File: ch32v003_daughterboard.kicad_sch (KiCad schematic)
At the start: 7 parts, among them J1 Conn_02x05_Odd_Even, J2 Conn_01x03_Pin, P1 Header 7X2, P2 Header 7X2

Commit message: free SDIO + pot.
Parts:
- added RV1: Mouser PTN091-V05115K1B, symbol Device:R_Potentiometer
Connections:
- net GND: now also RV1.3
- net PD0: now also BAR1.1 (A)
- net PD1: no longer BAR1.1 (A)
- net PD3: now also RV1.2
- net VCC: now also RV1.1
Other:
- moved on the sheet: C1, C2, J1, J2, P1, P2

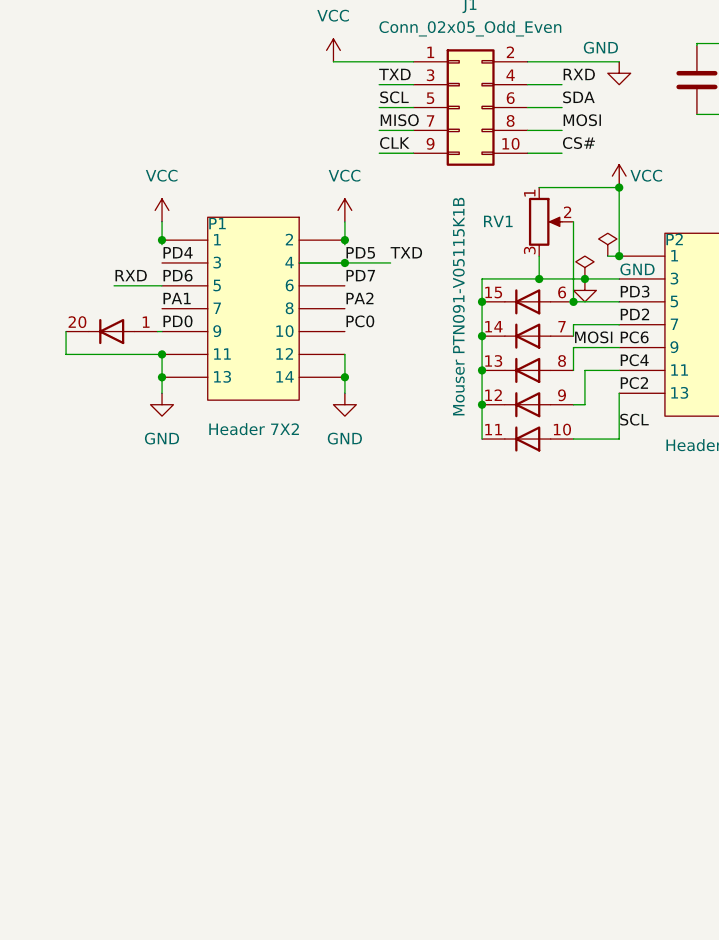
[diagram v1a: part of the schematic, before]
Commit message: add FTDI RS232-USB
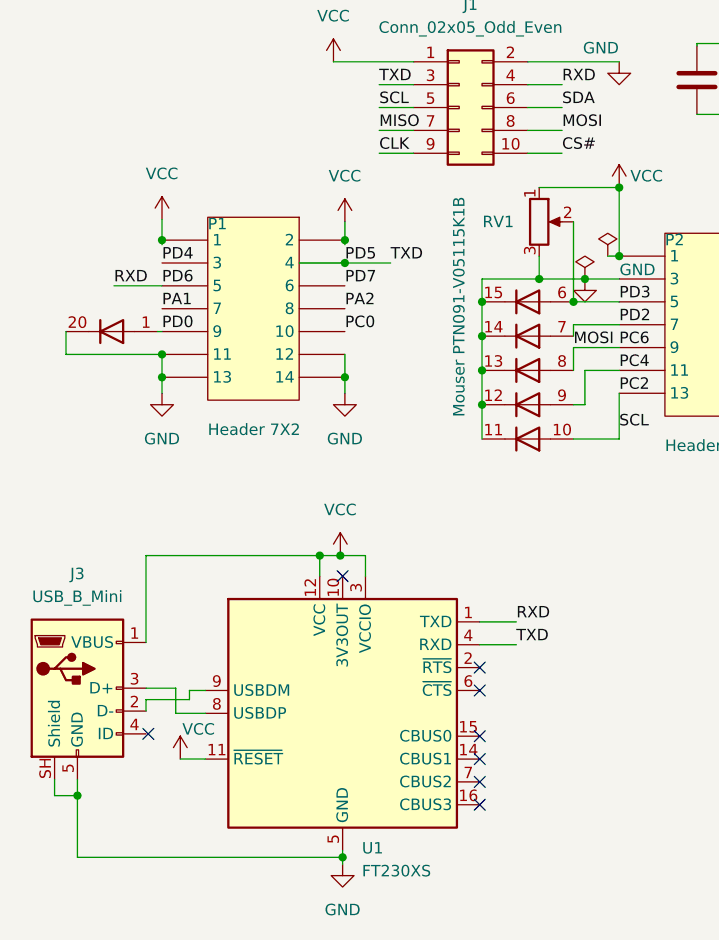
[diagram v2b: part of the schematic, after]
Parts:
- added J3: USB_B_Mini, Connector_USB:USB_Mini-B_Lumberg_2486_01_Horizontal, symbol Connector:USB_B_Mini
- added U1: FT230XS, Package_SO:SSOP-16_3.9x4.9mm_P0.635mm, symbol Interface_USB:FT230XS
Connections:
- net GND: now also J3.5 (GND), J3.SH (Shield), U1.13 (GND), U1.5 (GND)
- net PD5: now also U1.4 (RXD)
- net PD6: now also U1.1 (TXD)
- net VCC: now also J3.1 (VBUS), U1.11 (~{RESET}), U1.12 (VCC), U1.3 (VCCIO)
- new net: J3.3 (D+), U1.8 (USBDP)
- new net: J3.2 (D-), U1.9 (USBDM)
- no-connect marks 0 -> 8

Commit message: add push button
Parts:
- added R1: R, Resistor_SMD:R_0805_2012Metric_Pad1.20x1.40mm_HandSolder, symbol Device:R
- added SW1: SW_SPST, Button_Switch_SMD:SW_SPST_B3SL-1002P, symbol Switch:SW_SPST
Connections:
- net GND: now also SW1.2 (B)
- net PC0: now also R1.2, SW1.1 (A)
- net VCC: now also R1.1
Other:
- moved on the sheet: P1

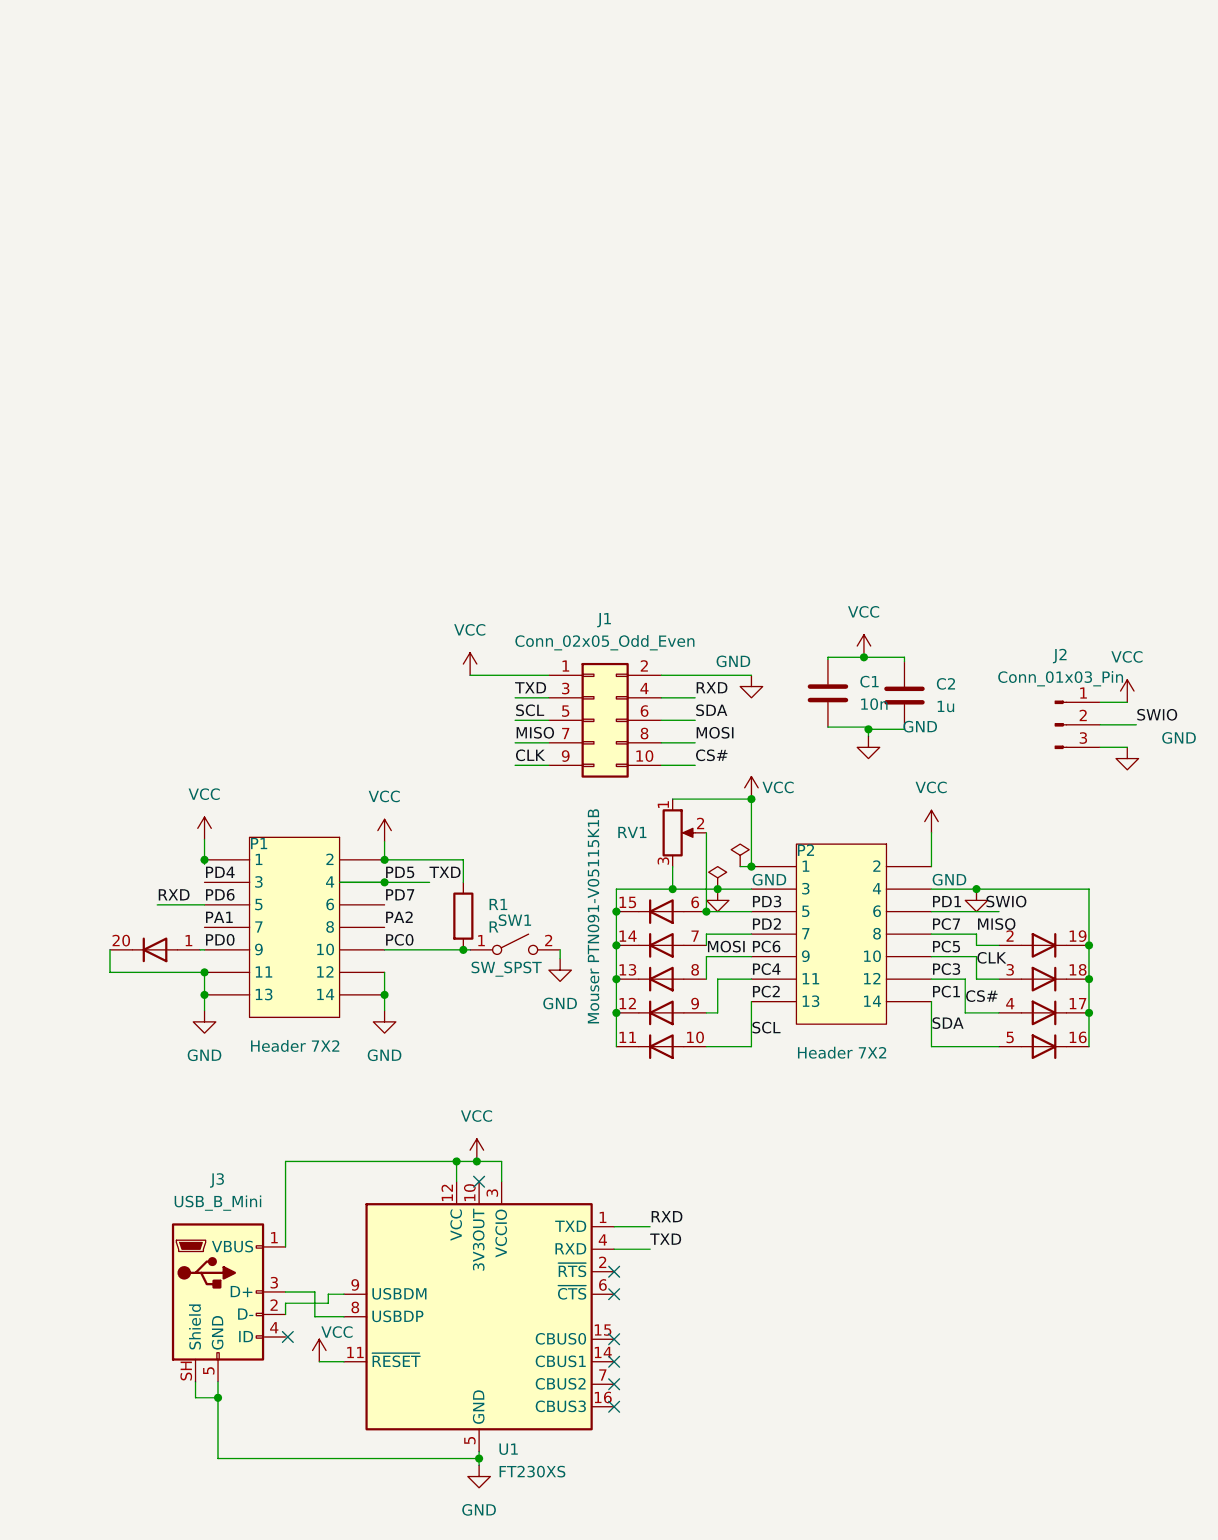
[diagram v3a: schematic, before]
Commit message: add I2C pullup resistors
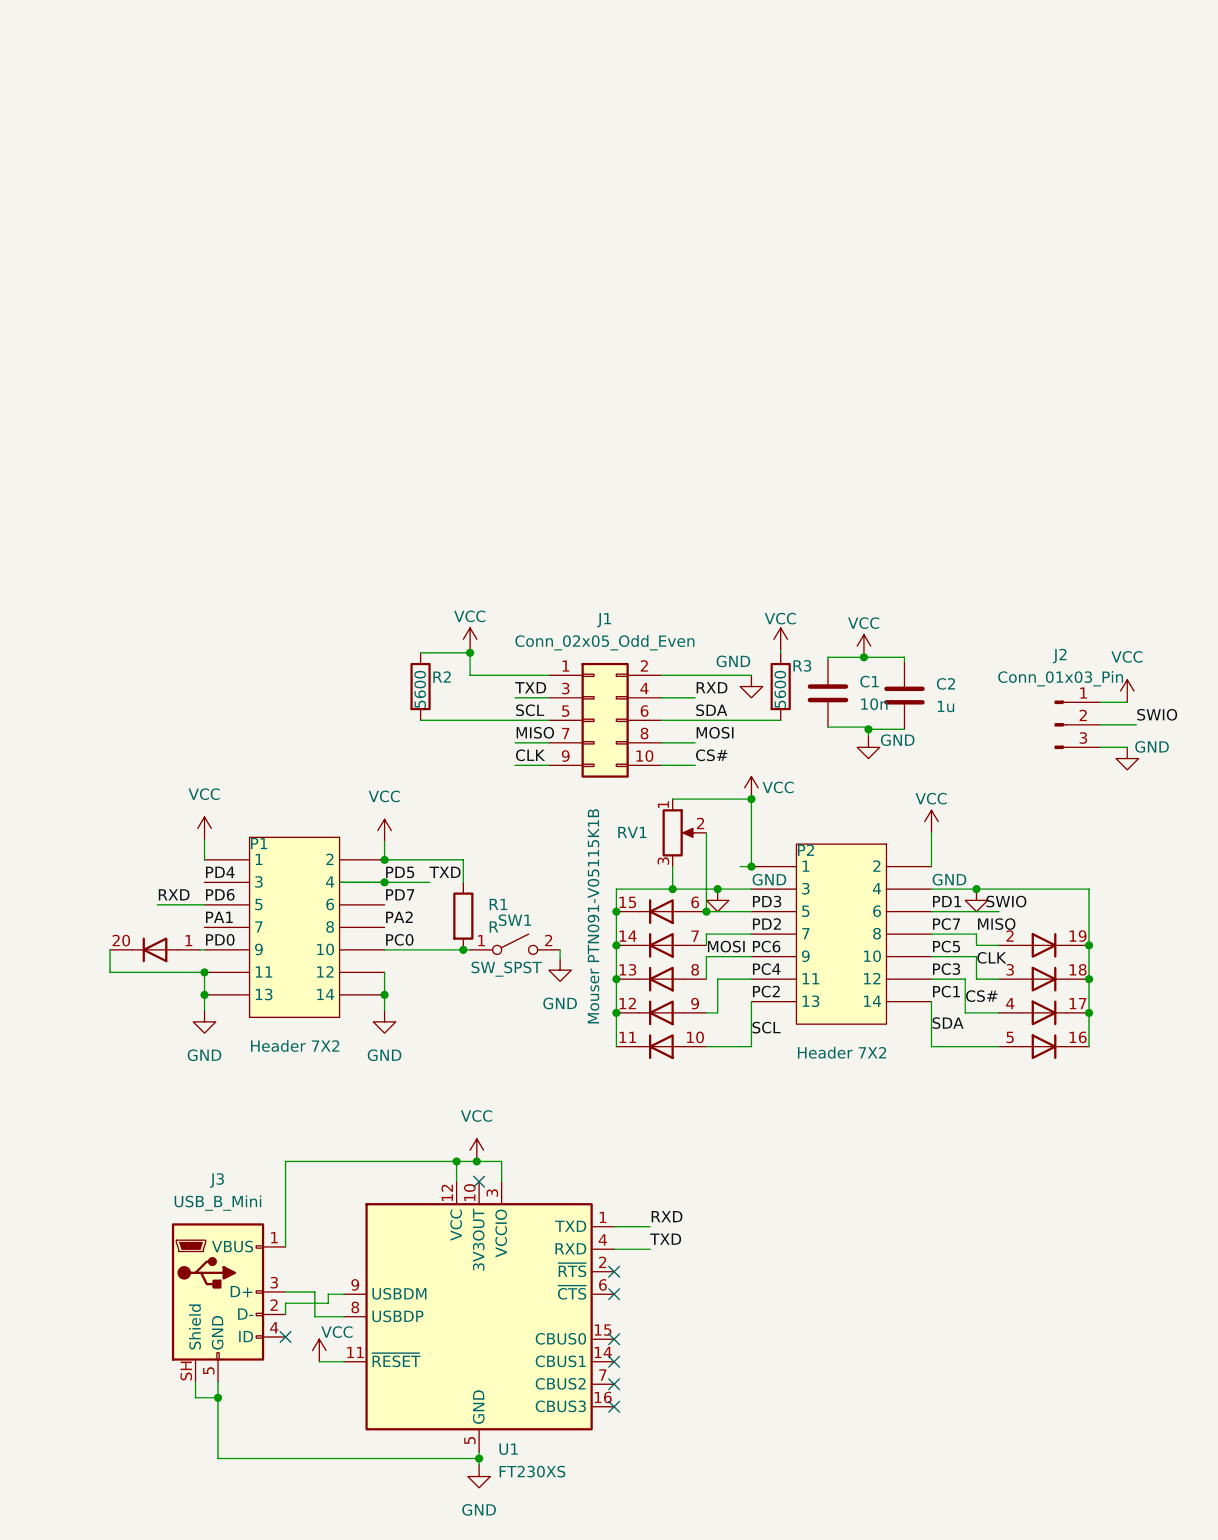
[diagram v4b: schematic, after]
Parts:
- added R2, R3: 5600, Resistor_SMD:R_0805_2012Metric_Pad1.20x1.40mm_HandSolder, symbol Device:R
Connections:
- net PC1: now also R3.2
- net PC2: now also R2.2
- net VCC: now also R2.1, R3.1

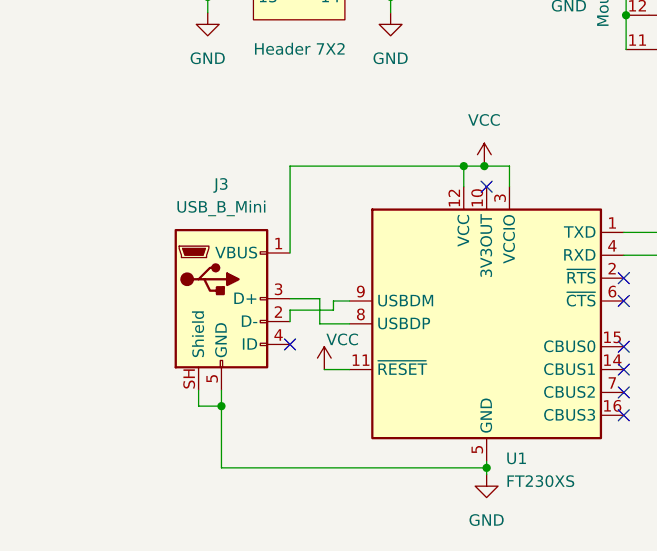
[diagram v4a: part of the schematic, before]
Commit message: add missing passive and decoupling capacitors
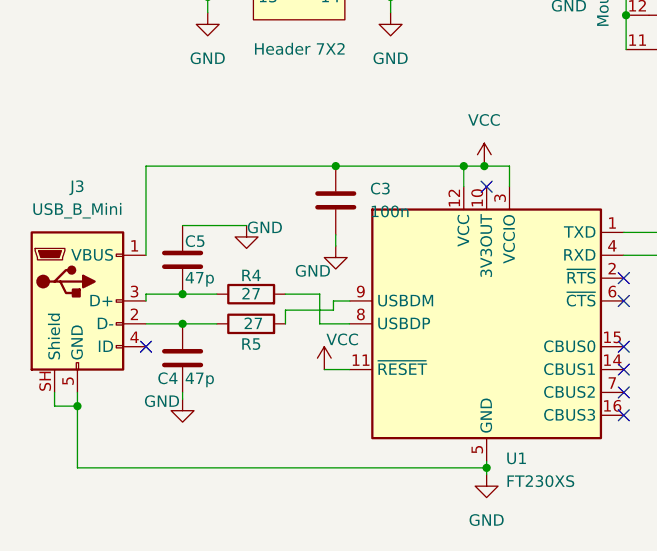
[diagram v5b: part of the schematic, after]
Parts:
- added C3: 100n, Capacitor_SMD:C_0805_2012Metric_Pad1.18x1.45mm_HandSolder, symbol Device:C
- added C4, C5: 47p, Capacitor_SMD:C_0805_2012Metric_Pad1.18x1.45mm_HandSolder, symbol Device:C
- added R4, R5: 27, Resistor_SMD:R_0805_2012Metric_Pad1.20x1.40mm_HandSolder, symbol Device:R
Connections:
- net GND: now also C3.2, C4.2, C5.1
- net VCC: now also C3.1
- net at J3.3 (D+): now also C5.2, R4.1; no longer U1.8 (USBDP)
- net at U1.9 (USBDM): now also R5.2; no longer J3.2 (D-)
- new net: R4.2, U1.8 (USBDP)
- new net: C4.1, J3.2 (D-), R5.1
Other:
- moved on the sheet: J3
